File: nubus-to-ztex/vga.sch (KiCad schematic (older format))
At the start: 20 parts, among them J4 DB15_Female_HighDensity_Mount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, U2 AD1580, U4 ADV7125-lqfp48

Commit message: large update
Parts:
- J4: MPN L77HDE15SD1CH4F -> L77HDE15SD1CH4FVGA; MPN-STD (none) -> L77HDE15SD1CH4F; URL https://www.mouser.fr/ProductDetail/Amphenol/L77HDE15SD1CH4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 -> https://www.mouser.fr/ProductDetail/Amphenol-Commercial-Pro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; URL-STD (none) -> https://www.mouser.fr/ProductDetail/Amphenol/L77HDE15SD1CH4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
- U2: MPN AD1580ARTZ -> AD1580BRTZ; MPN-STD (none) -> AD1580ARTZ; URL https://www.mouser.fr/ProductDetail/Analog-Devices/AD1580AR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 -> https://www.mouser.fr/ProductDetail/Analog-Devices/AD1580BR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; URL-STD (none) -> https://www.mouser.fr/ProductDetail/Analog-Devices/AD1580AR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
- U4: URL https://lcsc.com/product-detail/Digital-To-Analog-Converters-DACs_Analog-Devices-ADV7125KSTZ50_C514374.html -> https://lcsc.com/product-detail/Digital-To-Analog-Converters-DACs_Analog-Devices-ADV7125JSTZ240_C514373.html
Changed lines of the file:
@@
 $Descr A4 11693 8268
 encoding utf-8
-Sheet 4 7
+Sheet 7 7
 Title ""
 Date ""
@@
 F 2 "For_SeeedStudio:L77HDE15SD1CH4RHNVGA" H 6850 3750 50  0001 C CNN
 F 3 " ~" H 6850 3750 50  0001 C CNN
-F 4 "L77HDE15SD1CH4F" H 7800 3350 50  0001 C CNN "MPN"
-F 5 "https://www.mouser.fr/ProductDetail/Amphenol/L77HDE15SD1CH4F?qs=mq7kV%2Fq8lk6plQnZOUKCHg%3D%3D" H 7800 3350 50  0001 C CNN "URL"
+F 4 "L77HDE15SD1CH4F" H 7800 3350 50  0001 C CNN "MPN-STD"
+F 5 "https://www.mouser.fr/ProductDetail/Amphenol/L77HDE15SD1CH4F?qs=mq7kV%2Fq8lk6plQnZOUKCHg%3D%3D" H 7800 3350 50  0001 C CNN "URL-STD"
 F 6 "https://www.mouser.com/datasheet/2/18/1/HD_high_density-1501066.pdf" H 7800 3350 50  0001 C CNN "Amphenol Catalog"
 F 7 "4F, 4R, 3R, 3F: variations on the screw bits" H 7800 3350 50  0001 C CNN "Notes"
+F 8 "L77HDE15SD1CH4FVGA" H 7800 3350 50  0001 C CNN "MPN"
+F 9 "https://www.mouser.fr/ProductDetail/Amphenol-Commercial-Products/L77HDE15SD1CH4FVGA?qs=ToP8pWlZ0bNtQSp9f8k5Rw%3D%3D" H 7800 3350 50  0001 C CNN "URL"
 	1    7800 3350
 	1    0    0    -1
@@
 F 3 "https://www.mouser.fr/datasheet/2/609/ADV7125-1503638.pdf" H 4450 3850 50  0001 C CNN
 F 4 "ADV7125JSTZ240" H 4450 3850 50  0001 C CNN "MPN"
-F 5 "https://lcsc.com/product-detail/Digital-To-Analog-Converters-DACs_Analog-Devices-ADV7125KSTZ50_C514374.html" H 4450 3850 50  0001 C CNN "URL"
+F 5 "https://lcsc.com/product-detail/Digital-To-Analog-Converters-DACs_Analog-Devices-ADV7125JSTZ240_C514373.html" H 4450 3850 50  0001 C CNN "URL"
 	1    4450 3850
 	1    0    0    -1
@@
 F 2 "Package_TO_SOT_SMD:SOT-23" H 5950 2500 50  0001 C CNN
 F 3 "" H 5950 2500 50  0001 C CNN
-F 4 "AD1580ARTZ" H 5950 2500 50  0001 C CNN "MPN"
-F 5 "https://www.mouser.fr/ProductDetail/Analog-Devices/AD1580ARTZ-REEL7?qs=NmRFExCfTkENN3U3%252BacLbA%3D%3D" H 5950 2500 50  0001 C CNN "URL"
+F 4 "AD1580ARTZ" H 5950 2500 50  0001 C CNN "MPN-STD"
+F 5 "https://www.mouser.fr/ProductDetail/Analog-Devices/AD1580ARTZ-REEL7?qs=NmRFExCfTkENN3U3%252BacLbA%3D%3D" H 5950 2500 50  0001 C CNN "URL-STD"
+F 6 "AD1580BRTZ" H 5950 2500 50  0001 C CNN "MPN"
+F 7 "https://www.mouser.fr/ProductDetail/Analog-Devices/AD1580BRTZ-REEL7?qs=NmRFExCfTkFZVi9%2F1ZfkXg%3D%3D" H 5950 2500 50  0001 C CNN "URL"
 	1    5950 2500
 	1    0    0    -1

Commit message: large clean-up update
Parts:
- added C38: 1uF, Capacitor_SMD:C_0603_1608Metric, symbol Device:C
- U13: renamed from U2; MPN AD1580BRTZ -> AD1580ARTZ; MPN-ALT (none) -> AD1580BRTZ; MPN-STD AD1580ARTZ -> (none); URL https://www.mouser.fr/ProductDetail/Analog-Devices/AD1580BR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 -> https://www.mouser.fr/ProductDetail/Analog-Devices/AD1580AR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; URL-ALT (none) -> https://www.mouser.fr/ProductDetail/Analog-Devices/AD1580BR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; URL-STD https://www.mouser.fr/ProductDetail/Analog-Devices/AD1580AR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 -> (none)
- renumbered C32 to C30, C7 to C31, C6 to C32, C29 to C33, C8 to C34, C9 to C35, C5 to C36, C10 to C37, C11 to C39, J4 to J9, R3 to R28, R20 to R29, R1 to R30, R18 to R31, R19 to R32, R4 to R33, R5 to R34, R6 to R35, U4 to U12
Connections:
- wire segments 31 -> 33

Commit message: some missing stuff, minor HW update, SW
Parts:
- U13: MPN AD1580ARTZ -> AD1580BRTZ; MPN-ALT AD1580BRTZ -> AD1580ARTZ; URL https://www.mouser.fr/ProductDetail/Analog-Devices/AD1580AR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 -> https://www.digikey.fr/fr/products/detail/analog-devices-in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; URL-mouser (none) -> https://www.mouser.fr/ProductDetail/Analog-Devices/AD1580AR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
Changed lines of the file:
@@
 F 2 "Package_TO_SOT_SMD:SOT-23" H 5950 2500 50  0001 C CNN
 F 3 "" H 5950 2500 50  0001 C CNN
-F 4 "AD1580ARTZ" H 5950 2500 50  0001 C CNN "MPN"
-F 5 "https://www.mouser.fr/ProductDetail/Analog-Devices/AD1580ARTZ-REEL7?qs=NmRFExCfTkENN3U3%252BacLbA%3D%3D" H 5950 2500 50  0001 C CNN "URL"
-F 6 "AD1580BRTZ" H 5950 2500 50  0001 C CNN "MPN-ALT"
+F 4 "AD1580BRTZ" H 5950 2500 50  0001 C CNN "MPN"
+F 5 "https://www.mouser.fr/ProductDetail/Analog-Devices/AD1580ARTZ-REEL7?qs=NmRFExCfTkENN3U3%252BacLbA%3D%3D" H 5950 2500 50  0001 C CNN "URL-mouser"
+F 6 "AD1580ARTZ" H 5950 2500 50  0001 C CNN "MPN-ALT"
 F 7 "https://www.mouser.fr/ProductDetail/Analog-Devices/AD1580BRTZ-REEL7?qs=NmRFExCfTkFZVi9%2F1ZfkXg%3D%3D" H 5950 2500 50  0001 C CNN "URL-ALT"
+F 8 "https://www.digikey.fr/fr/products/detail/analog-devices-inc/AD1580BRTZ-REEL7/936475" H 5950 2500 50  0001 C CNN "URL"
 	1    5950 2500
 	1    0    0    -1

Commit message: drop vga
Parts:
- removed C30, C31, C32, C33: 100nF, Capacitor_SMD:C_0603_1608Metric, symbol Device:C
- removed C34, C35, C36: 10nF, Capacitor_SMD:C_0603_1608Metric, symbol Device:C
- removed C37, C38: 1uF, Capacitor_SMD:C_0603_1608Metric, symbol Device:C
- removed J9: DB15_Female_HighDensity_MountingHoles, For_SeeedStudio:L77HDE15SD1CH4RHNVGA, symbol Connector:DB15_Female_HighDensity_MountingHoles
- removed R28: 536, Resistor_SMD:R_0603_1608Metric, symbol Device:R
- removed R29: 1k, Resistor_SMD:R_0603_1608Metric, symbol Device:R
- removed R30, R31, R32: 75, Resistor_SMD:R_0603_1608Metric, symbol Device:R
- removed R34, R35: 100, Resistor_SMD:R_0603_1608Metric, symbol Device:R
- removed U12: ADV7125-lqfp48, For_SeeedStudio:ADV7125KSTZ140, symbol ADV7125-lqfp48:ADV7125-lqfp48
- removed U13: AD1580, Package_TO_SOT_SMD:SOT-23, symbol ad1580:AD1580
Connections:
- net labels removed: +3V3, FPGA_B0, FPGA_B1, FPGA_B2, FPGA_B3, FPGA_B4, FPGA_B5, FPGA_B6, FPGA_B7, FPGA_G0, FPGA_G1, FPGA_G2, FPGA_G3, FPGA_G4, FPGA_G5, FPGA_G6, FPGA_G7, FPGA_R0, FPGA_R1, FPGA_R2, FPGA_R3, FPGA_R4, FPGA_R5, FPGA_R6, FPGA_R7, FPGA_VGA_CLK, FPGA_VGA_HS, FPGA_VGA_VS, VGA_B, VGA_G, VGA_HS, VGA_R, VGA_VS, blank, blankb, comp, psaveb, rset, vref
- wire segments 33 -> 2
- no-connect marks 6 -> 0
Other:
- note removed: "A 0.1 uF ceramic capacitor must be connected between COMP and VAA.\n"
- note removed: "A resistor (RSET) connected between this pin and GND controls the magnitude of the full-scale video signal."
- note removed: "If sync information is not required on the green channel, the SYNC input should be tied to Logic 0."
- note removed: "Reduced power consumption is available on the ADV7125 when this pin is active."
- note removed: "While BLANK is a Logic 0, the R0 to R7, G0 to G7, and B0 to B7 pixel inputs are ignored."
- moved on the sheet: C39, R33

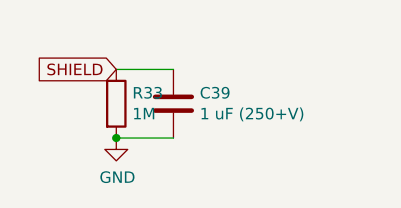
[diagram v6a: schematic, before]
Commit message: merge pmod & leds into an extended pmod on the outside. Also some BoM updates.
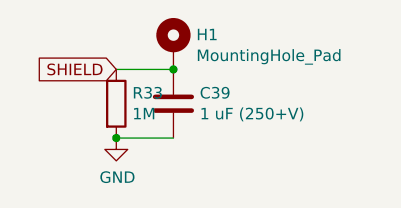
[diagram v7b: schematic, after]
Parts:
- added H1: MountingHole_Pad, MountingHole:MountingHole_2.2mm_M2_Pad, symbol Mechanical:MountingHole_Pad
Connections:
- net SHIELD: now also H1.1
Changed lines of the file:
@@
 $Descr A4 11693 8268
 encoding utf-8
-Sheet 7 10
+Sheet 7 9
 Title "nubus-to-ztex VGA"
 Date ""
@@
 	1    0    0    -1
 $EndComp
+$Comp
+L Mechanical:MountingHole_Pad H1
+U 1 1 633638E3
+P 8250 4800
+F 0 "H1" H 8350 4851 50  0000 L CNN
+F 1 "MountingHole_Pad" H 8350 4760 50  0000 L CNN
+F 2 "MountingHole:MountingHole_2.2mm_M2_Pad" H 8250 4800 50  0001 C CNN
+F 3 "~" H 8250 4800 50  0001 C CNN
+	1    8250 4800
+	1    0    0    -1
+$EndComp
+Connection ~ 8250 4900
 $EndSCHEMATC

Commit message: move shielding to hdmi, trace cleanup
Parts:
- removed C39: 1 uF (250+V), Capacitor_THT:CP_Radial_D6.3mm_P2.50mm, symbol Device:C
- removed H1: MountingHole_Pad, MountingHole:MountingHole_2.2mm_M2_Pad, symbol Mechanical:MountingHole_Pad
- removed R33: 1M, Resistor_SMD:R_1210_3225Metric, symbol Device:R
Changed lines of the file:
@@
 Comment4 ""
 $EndDescr
-Text GLabel 8000 4900 0    50   Input ~ 0
-SHIELD
-$Comp
-L power:GND #PWR0131
-U 1 1 61988E37
-P 8000 5200
-F 0 "#PWR0131" H 8000 4950 50  0001 C CNN
-F 1 "GND" H 8005 5027 50  0000 C CNN
-F 2 "" H 8000 5200 50  0001 C CNN
-F 3 "" H 8000 5200 50  0001 C CNN
-	1    8000 5200
-	1    0    0    -1
-$EndComp
-Wire Wire Line
-	8250 5200 8000 5200
-Wire Wire Line
-	8250 4900 8000 4900
-$Comp
-L Device:C C39
-U 1 1 619889C3
-P 8250 5050
-F 0 "C39" H 8365 5096 50  0000 L CNN
-F 1 "1 uF (250+V)" H 8365 5005 50  0000 L CNN
-F 2 "Capacitor_THT:CP_Radial_D6.3mm_P2.50mm" H 8288 4900 50  0001 C CNN
-F 3 "~" H 8250 5050 50  0001 C CNN
-F 4 "860021373002" H 8250 5050 50  0001 C CNN "MPN-ALT"
-F 5 "https://www2.mouser.com/ProductDetail/Wurth-Elektronik/860021373002?qs=0KOYDY2FL28tNXbPyU6hsg%3D%3D" H 8250 5050 50  0001 C CNN "URL-ALT"
-F 6 "KM010M400E110A" H 8250 5050 50  0001 C CNN "MPN"
-F 7 "https://lcsc.com/product-detail/Aluminum-Electrolytic-Capacitors-Leaded_Capxon-International-Elec-KM010M400E110A_C59365.html" H 8250 5050 50  0001 C CNN "URL"
-	1    8250 5050
-	1    0    0    -1
-$EndComp
-Connection ~ 8000 5200
-$Comp
-L Device:R R33
-U 1 1 61988921
-P 8000 5050
-F 0 "R33" H 8070 5096 50  0000 L CNN
-F 1 "1M" H 8070 5005 50  0000 L CNN
-F 2 "Resistor_SMD:R_1210_3225Metric" V 7930 5050 50  0001 C CNN
-F 3 "~" H 8000 5050 50  0001 C CNN
-F 4 "RC1210FR-071ML" H 8000 5050 50  0001 C CNN "MPN-ALT"
-F 5 "https://lcsc.com/product-detail/Chip-Resistor-Surface-Mount_YAGEO-RC1210FR-071ML_C470029.html" H 8000 5050 50  0001 C CNN "URL-ALT"
-F 6 "1210W2F1004T5E" H 8000 5050 50  0001 C CNN "MPN"
-F 7 "https://www.lcsc.com/product-detail/Chip-Resistor-Surface-Mount_UNI-ROYAL-Uniroyal-Elec-1210W2F1004T5E_C620664.html" H 8000 5050 50  0001 C CNN "URL"
-	1    8000 5050
-	1    0    0    -1
-$EndComp
-$Comp
-L Mechanical:MountingHole_Pad H1
-U 1 1 633638E3
-P 8250 4800
-F 0 "H1" H 8350 4851 50  0000 L CNN
-F 1 "MountingHole_Pad" H 8350 4760 50  0000 L CNN
-F 2 "MountingHole:MountingHole_2.2mm_M2_Pad" H 8250 4800 50  0001 C CNN
-F 3 "~" H 8250 4800 50  0001 C CNN
-	1    8250 4800
-	1    0    0    -1
-$EndComp
-Connection ~ 8250 4900
 $EndSCHEMATC
